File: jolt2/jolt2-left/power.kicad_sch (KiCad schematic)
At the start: 9 parts, among them J29 USB_C_Receptacle_USB2.0_14P, J30 Conn_ARM_JTAG_SWD_10

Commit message: jolt2: Prepare rev A
This is Rev A, being sent for production.
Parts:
- J29: footprint Connector_USB:USB_C_Receptacle_GCT_USB4085 -> davidb-keyboard-foot:USB_C_Receptacle_GCT_USB4085
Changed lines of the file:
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@@
 			)
 		)
-		(property "Footprint" "Connector_USB:USB_C_Receptacle_GCT_USB4085"
+		(property "Footprint" "davidb-keyboard-foot:USB_C_Receptacle_GCT_USB4085"
 			(at 55.88 66.04 0)
 			(effects

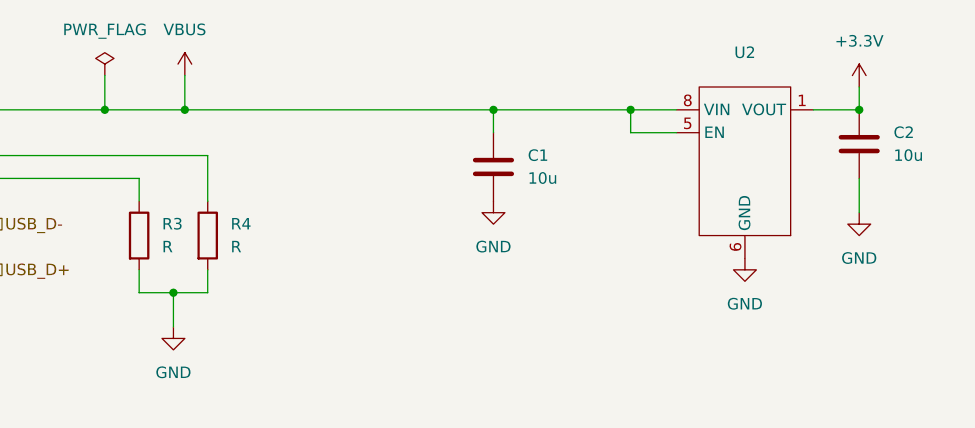
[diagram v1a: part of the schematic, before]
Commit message: Various PCB updates
This is before fixing the footprint for the WS2812. Turns out there is a
ws2812 MINI, and a MINI-HS, and they have very different footprints.
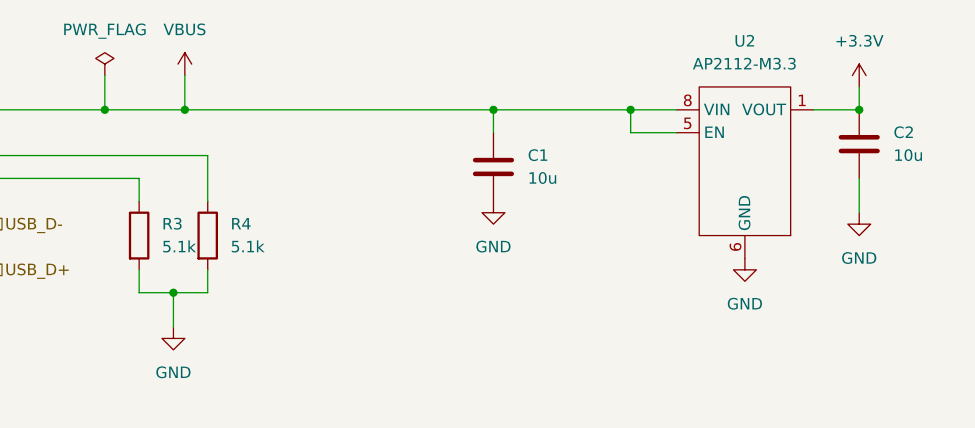
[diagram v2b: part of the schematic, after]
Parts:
- D2: now left out of the parts list
- R3, R4: value R -> 5.1k
- U2: value ~ -> AP2112-M3.3
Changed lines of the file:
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@@
 		(unit 1)
 		(exclude_from_sim no)
-		(in_bom yes)
+		(in_bom no)
 		(on_board yes)
 		(dnp no)
@@
 		(fields_autoplaced yes)
 		(property "Reference" "U2"
-			(at 156.21 44.45 0)
-			(effects
-				(font
-					(size 1.27 1.27)
-				)
-			)
-		)
-		(property "Value" "~"
-			(at 156.21 46.99 0)
+			(at 156.21 43.18 0)
+			(effects
+				(font
+					(size 1.27 1.27)
+				)
+			)
+		)
+		(property "Value" "AP2112-M3.3"
+			(at 156.21 45.72 0)
 			(effects
 				(font
@@
 			)
 		)
-		(property "Value" "R"
+		(property "Value" "5.1k"
 			(at 99.06 66.0399 0)
 			(effects
@@
 			)
 		)
-		(property "Value" "R"
+		(property "Value" "5.1k"
 			(at 91.44 66.0399 0)
 			(effects

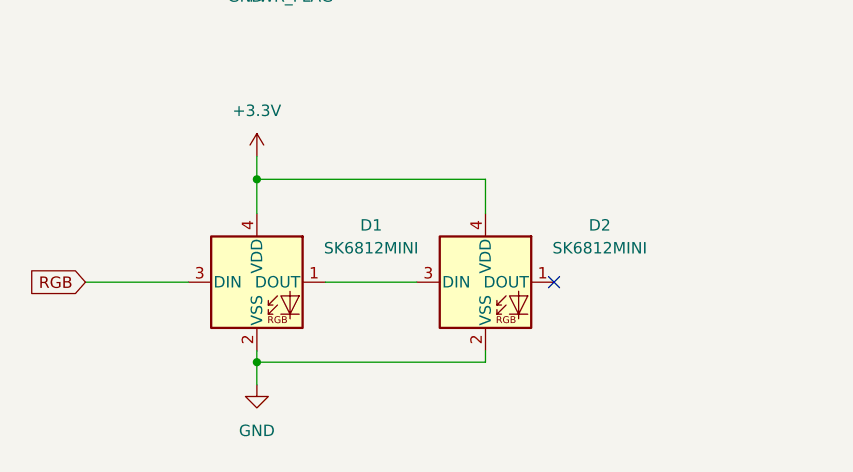
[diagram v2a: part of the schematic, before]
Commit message: jolt2-left: Fix symbol and footprint for ws2812
The ws2812 has both a MINI and a MINI-HS footprint, and they have rather
different footprints.  Update the symbol and draw a footprint for the
proper one we have purchased.
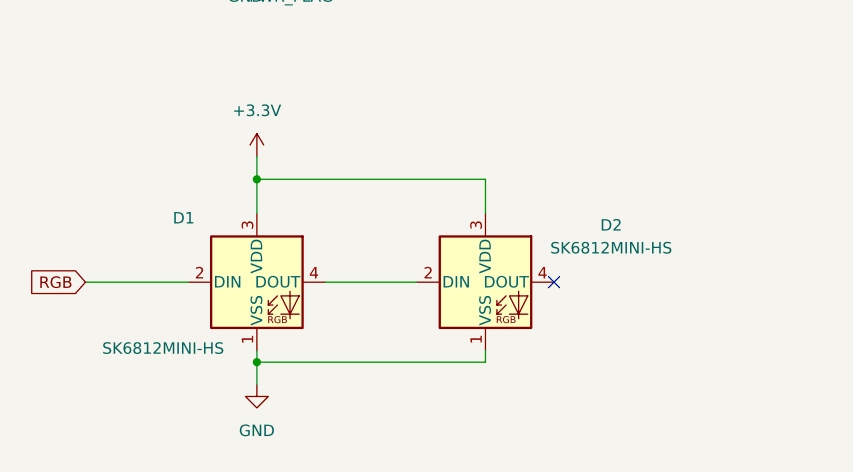
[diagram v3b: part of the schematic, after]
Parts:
- D1: value SK6812MINI -> SK6812MINI-HS; footprint LED_SMD:LED_SK6812MINI_PLCC4_3.5x3.5mm_P1.75mm -> davidb-keyboard-foot:SK6812-MINI-HS; symbol LED:SK6812MINI -> David Brown Keyboard Parts:SK6812MINI-HS
- D2: value SK6812MINI -> SK6812MINI-HS; footprint LED_SMD:LED_SK6812MINI_PLCC4_3.5x3.5mm_P1.75mm -> davidb-keyboard-foot:SK6812-MINI-HS; symbol LED:SK6812MINI -> David Brown Keyboard Parts:SK6812MINI-HS; now in the parts list
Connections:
- net +3.3V: now also D1.3 (VDD), D2.3 (VDD); no longer D1.4 (VDD), D2.4 (VDD)
- net GND: now also D1.1 (VSS), D2.1 (VSS); no longer D1.2 (VSS), D2.2 (VSS)
- net RGB: now also D1.2 (DIN); no longer D1.3 (DIN)
- new net: D1.4 (DOUT), D2.2 (DIN)
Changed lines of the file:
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@@
 	)
 	(symbol
-		(lib_id "LED:SK6812MINI")
+		(lib_id "David Brown Keyboard Parts:SK6812MINI-HS")
 		(at 78.74 125.73 0)
 		(unit 1)
 		(exclude_from_sim no)
-		(in_bom no)
+		(in_bom yes)
 		(on_board yes)
 		(dnp no)
 		(fields_autoplaced yes)
 		(property "Reference" "D2"
-			(at 91.44 119.4114 0)
-			(effects
-				(font
-					(size 1.27 1.27)
-				)
-			)
-		)
-		(property "Value" "SK6812MINI"
-			(at 91.44 121.9514 0)
-			(effects
-				(font
-					(size 1.27 1.27)
-				)
-			)
-		)
-		(property "Footprint" "LED_SMD:LED_SK6812MINI_PLCC4_3.5x3.5mm_P1.75mm"
+			(at 92.71 119.4114 0)
+			(effects
+				(font
+					(size 1.27 1.27)
+				)
+			)
+		)
+		(property "Value" "SK6812MINI-HS"
+			(at 92.71 121.9514 0)
+			(effects
+				(font
+					(size 1.27 1.27)
+				)
+			)
+		)
+		(property "Footprint" "davidb-keyboard-foot:SK6812-MINI-HS"
 			(at 80.01 133.35 0)
 			(effects
@@
 	)
 	(symbol
-		(lib_id "LED:SK6812MINI")
+		(lib_name "SK6812MINI-HS_1")
+		(lib_id "David Brown Keyboard Parts:SK6812MINI-HS")
 		(at 53.34 125.73 0)
 		(unit 1)
@@
 		(on_board yes)
 		(dnp no)
-		(fields_autoplaced yes)
 		(property "Reference" "D1"
-			(at 66.04 119.4114 0)
-			(effects
-				(font
-					(size 1.27 1.27)
-				)
-			)
-		)
-		(property "Value" "SK6812MINI"
-			(at 66.04 121.9514 0)
-			(effects
-				(font
-					(size 1.27 1.27)
-				)
-			)
-		)
-		(property "Footprint" "LED_SMD:LED_SK6812MINI_PLCC4_3.5x3.5mm_P1.75mm"
+			(at 45.212 118.618 0)
+			(effects
+				(font
+					(size 1.27 1.27)
+				)
+			)
+		)
+		(property "Value" "SK6812MINI-HS"
+			(at 42.926 133.096 0)
+			(effects
+				(font
+					(size 1.27 1.27)
+				)
+			)
+		)
+		(property "Footprint" "davidb-keyboard-foot:SK6812-MINI-HS"
 			(at 54.61 133.35 0)
 			(effects
